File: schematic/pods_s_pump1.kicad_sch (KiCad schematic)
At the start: 6 parts, among them M1 PUMP-5V-1A, Q1 IRLZ44N

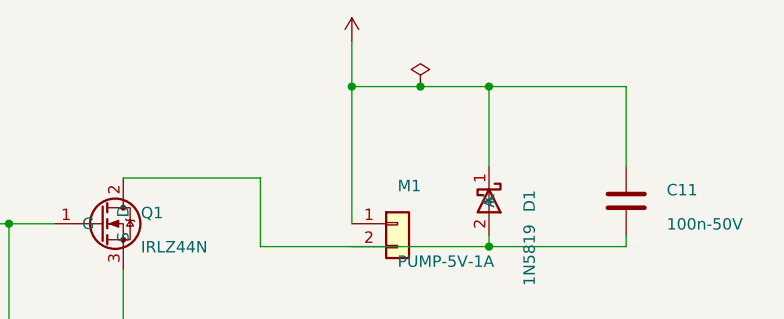
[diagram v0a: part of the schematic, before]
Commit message: Split PUMP_5V/LED_5V rails per SKiDL truth; flat draft guard
Pump/LED sheets used power:+5V symbols, joining the separately-fused
F2/F3 branches. Now PUMP_5V/LED_5V global labels; netlists match
pods.net pin-for-pin (full compare zero). pods.py flatness=1.0 so the
SKiDL draft can never clobber placed pods_s_* sheets. Docs net names.
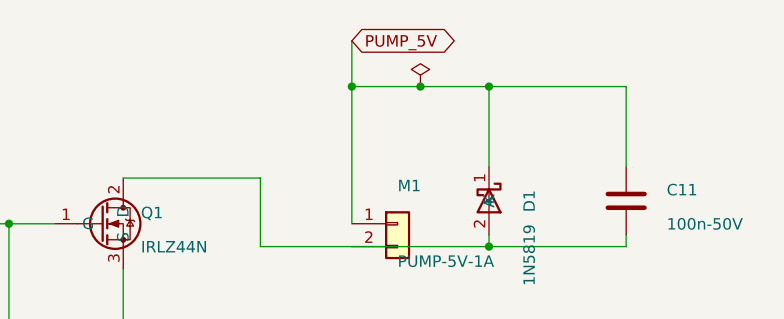
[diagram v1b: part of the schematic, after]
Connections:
- net +5V renamed PUMP_5V
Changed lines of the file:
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@@
   (junction (at 99.06 88.9) (diameter 0) (color 0 0 0 0)
 )
-  (symbol
-    (lib_id "power:+5V")
+  (global_label "PUMP_5V"
+    (shape bidirectional)
     (at 124.46 53.34 0)
-    (unit 1)
-    (exclude_from_sim no)
-    (in_bom no)
-    (on_board yes)
-    (dnp no)
-    (fields_autoplaced no)
-    (property "Reference" "#+5V04"
-      (at 124.46 53.34 0)
-      (effects (font (size 1.27 1.27)) (hide yes)))
-    (property "Value" "+5V"
-      (at 124.46 53.34 0)
-      (effects (font (size 1.27 1.27)) (hide yes)))
-    (pin "1"
+    (effects (font (size 1.27 1.27)) (justify left))
 )
-    (instances
-      (project "GrowMate"
-        (path "/216fdad8-4006-4d85-8157-93191bd90b6a/6a7fc3da-a420-529d-b2e9-45718d2c3adc"
-          (reference "#+5V04")
-          (unit 1)))))
   (wire
     (pts
@@
     (dnp no)
     (fields_autoplaced no)
-    (property "Reference" "#PWR05"
+    (property "Reference" "#PWR04"
       (at 132.08 58.42 0)
       (effects (font (size 1.27 1.27)) (hide yes)))
@@
       (project "GrowMate"
         (path "/216fdad8-4006-4d85-8157-93191bd90b6a/6a7fc3da-a420-529d-b2e9-45718d2c3adc"
-          (reference "#PWR05")
+          (reference "#PWR04")
           (unit 1)))))
   (junction (at 132.08 58.42) (diameter 0) (color 0 0 0 0)

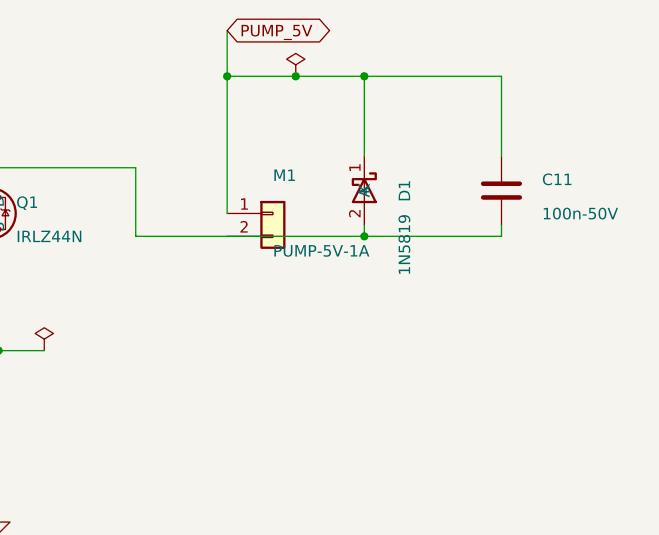
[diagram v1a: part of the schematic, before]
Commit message: Audit fixes: doc footprint strings, GPIO33 LED note, D1 1N5822
04-wiring footprint column now matches pods.py/BOM (U2/SW1/M1/D2).
GPIO33 red-LED load disclosed like GPIO4. Pump flyback 1N5819 -> 1N5822
(DO-41, 3A class for 2A stall turn-off). ERC gate holds, full netlist
compare zero, PDF/final refreshed.
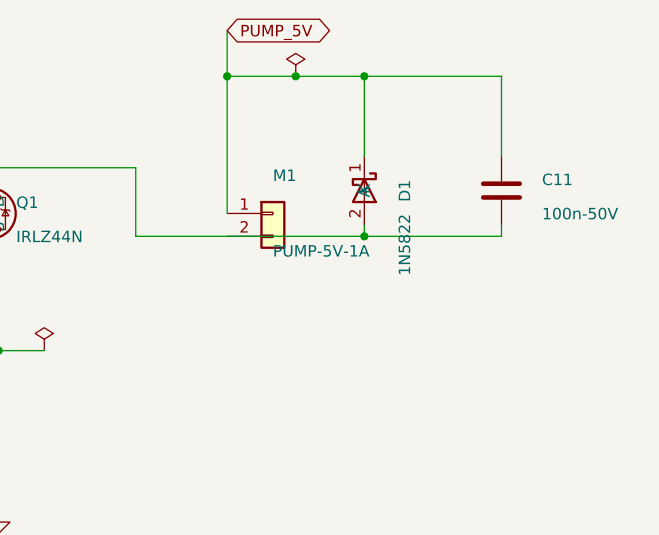
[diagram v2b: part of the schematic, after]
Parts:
- D1: value 1N5819 -> 1N5822
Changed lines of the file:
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@@
       (at 144.2 69.92 0)
       (effects (font (size 1.27 1.27)) (justify left)))
-    (property "Value" "1N5819"
+    (property "Value" "1N5822"
       (at 144.2 73.72 0)
       (effects (font (size 1.27 1.27)) (justify left)))

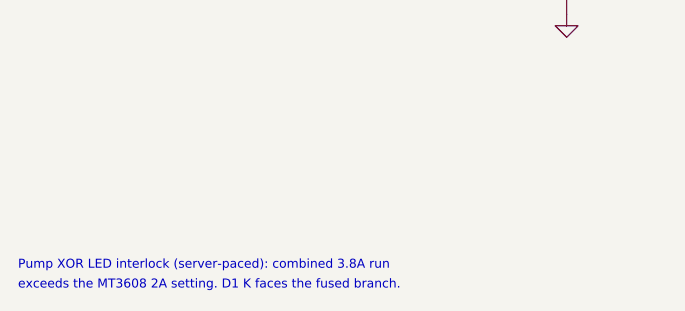
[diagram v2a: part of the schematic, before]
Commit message: Owner decisions: OUT+/- rewire (CELL_NEG), XL6009 boost, server XOR
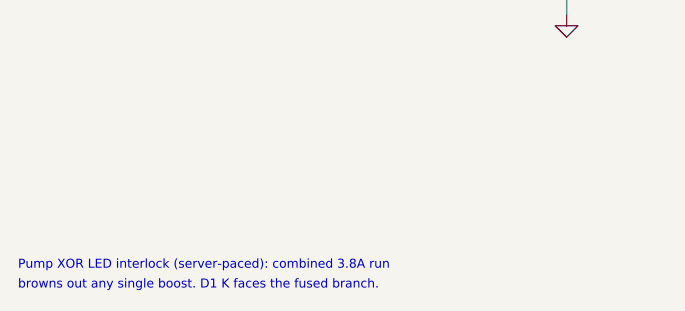
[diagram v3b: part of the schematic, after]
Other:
- note added: "browns out any single boost. D1 K faces the fused branch."
- note removed: "exceeds the MT3608 2A setting. D1 K faces the fused branch."
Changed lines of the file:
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@@
     (effects (font (size 1.0 1.0)) (justify left))
 )
-  (text "exceeds the MT3608 2A setting. D1 K faces the fused branch."
+  (text "browns out any single boost. D1 K faces the fused branch."
     (at 25.4 141.9 0)
     (effects (font (size 1.0 1.0)) (justify left))
